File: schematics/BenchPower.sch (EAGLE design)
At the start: 29 parts, among them U1 V_REG_317SINK, X2 9090-4R

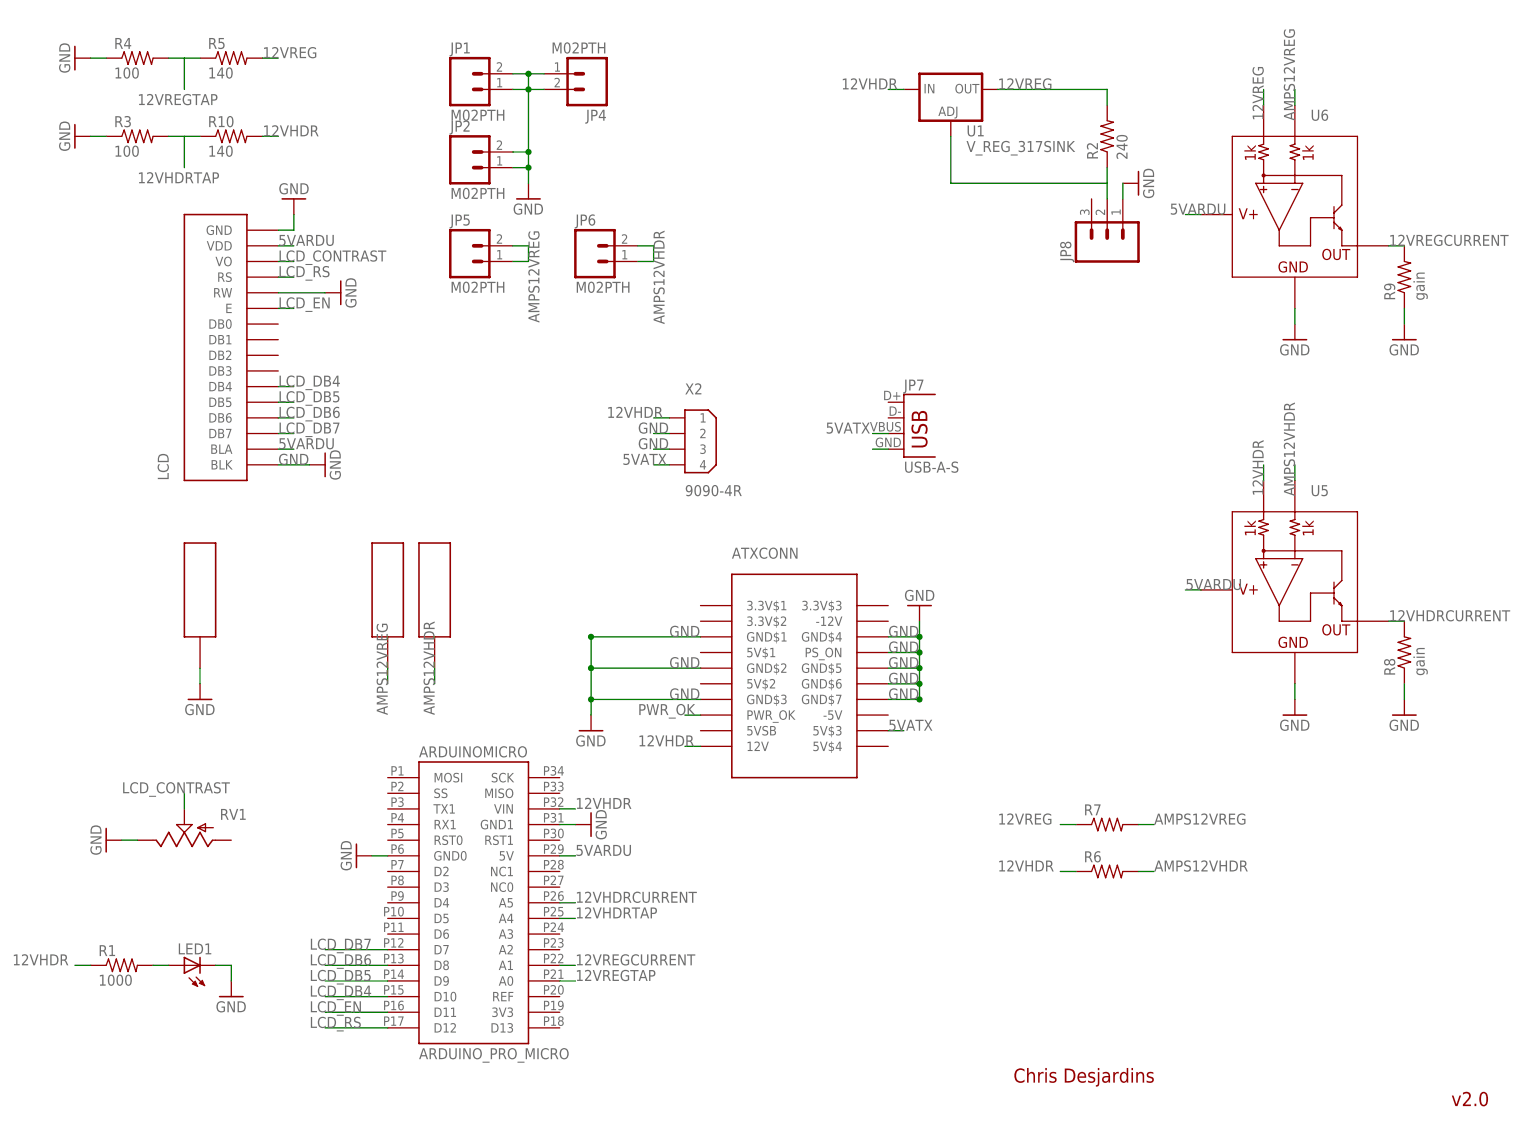
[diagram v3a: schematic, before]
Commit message: Reroute the lcd
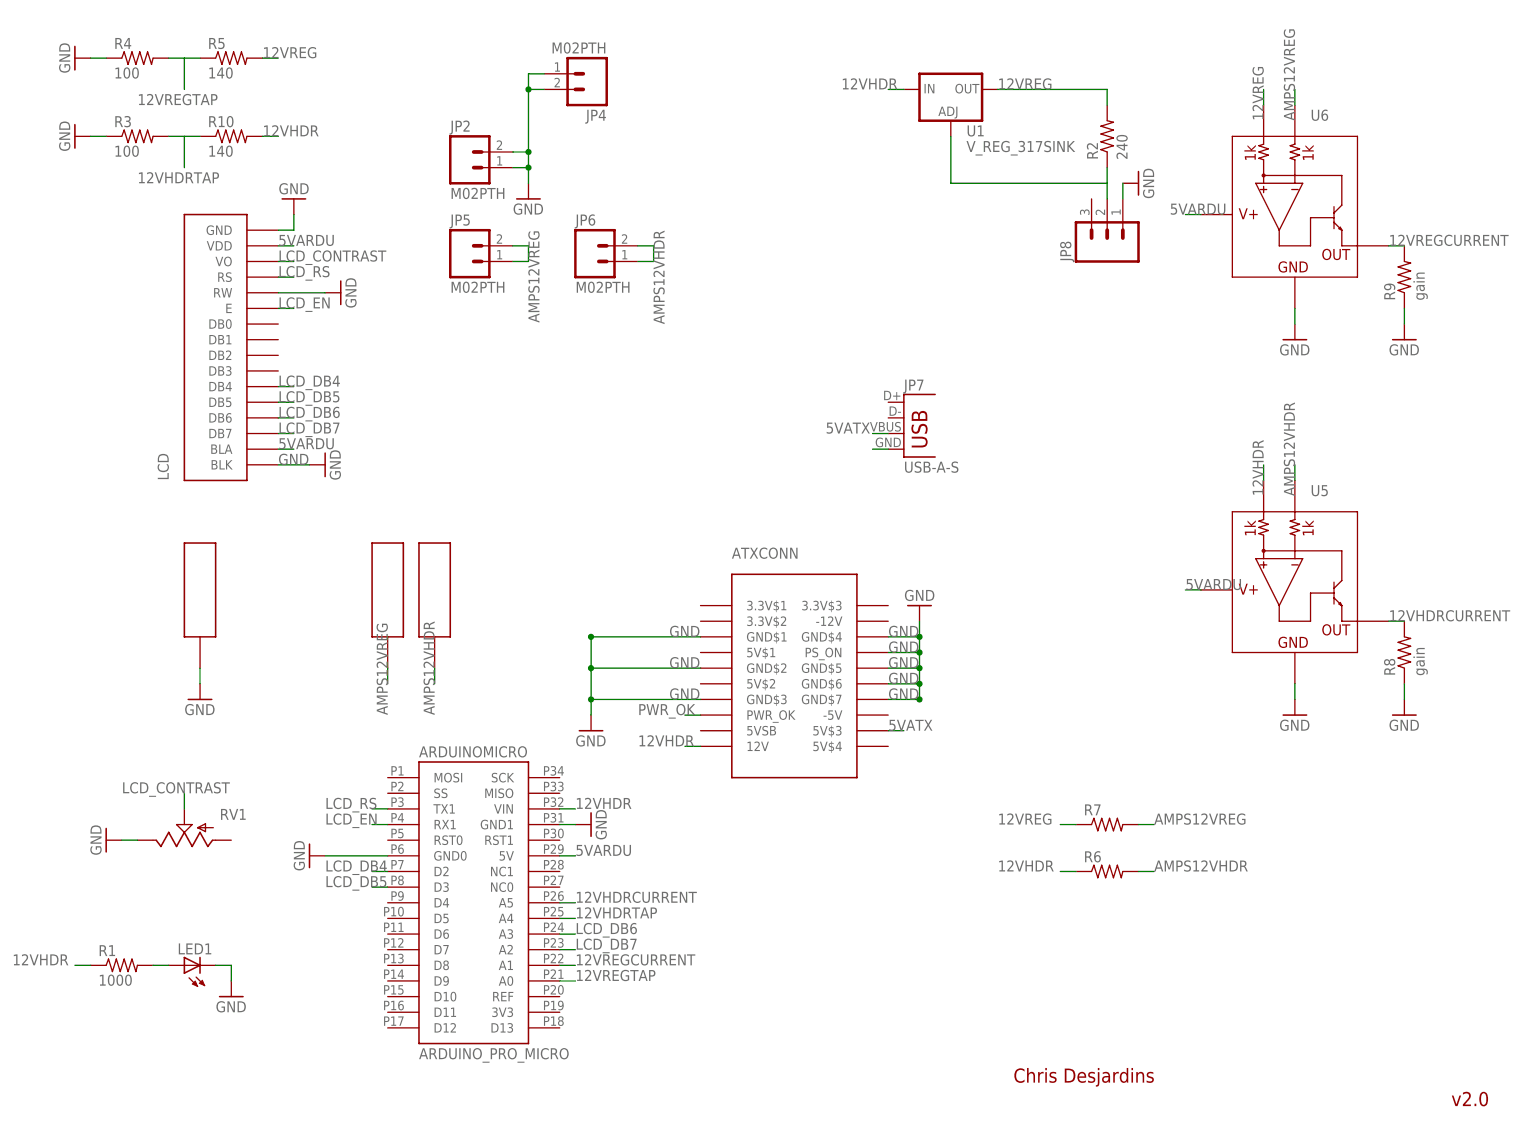
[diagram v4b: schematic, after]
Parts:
- removed JP1: M02PTH, SparkFun-Connectors:M02PTH
- removed X2: 9090-4R, con-thomas-betts:9090-4R
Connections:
- net 12VHDR: no longer X2.1
- net 5VATX: no longer X2.4
- net GND: no longer JP1.1, JP1.2, X2.2, X2.3
- net LCD_DB4: now also ARDUINOMICRO.D2; no longer ARDUINOMICRO.D10
- net LCD_DB5: now also ARDUINOMICRO.D3; no longer ARDUINOMICRO.D9
- net LCD_DB6: now also ARDUINOMICRO.A3; no longer ARDUINOMICRO.D8
- net LCD_DB7: now also ARDUINOMICRO.A2; no longer ARDUINOMICRO.D7
- net LCD_EN: now also ARDUINOMICRO.RX1; no longer ARDUINOMICRO.D11
- net LCD_RS: now also ARDUINOMICRO.TX1; no longer ARDUINOMICRO.D12
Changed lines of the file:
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@@
 <part name="U$5" library="desjardins" deviceset="BINDINGPOST" device=""/>
 <part name="GND1" library="SparkFun-Aesthetics" deviceset="GND" device=""/>
-<part name="X2" library="con-thomas-betts" deviceset="9090-4" device="R"/>
 <part name="ATXCONN" library="desjardins" deviceset="ATXPOWER" device=""/>
 <part name="ARDUINOMICRO" library="ChrisD" deviceset="ARDUINO_PRO_MICRO" device=""/>
@@
 <part name="GND17" library="SparkFun-Aesthetics" deviceset="GND" device=""/>
 <part name="GND18" library="SparkFun-Aesthetics" deviceset="GND" device=""/>
-<part name="JP1" library="SparkFun-Connectors" deviceset="M02" device="PTH"/>
 <part name="U5" library="SparkFun-AnalogIC" deviceset="INA139" device=""/>
 <part name="U6" library="SparkFun-AnalogIC" deviceset="INA139" device=""/>
@@
 <instance part="U$5" gate="G$1" x="33.02" y="91.44"/>
 <instance part="GND1" gate="1" x="33.02" y="73.66"/>
-<instance part="X2" gate="G$1" x="111.76" y="114.3"/>
 <instance part="ATXCONN" gate="G$1" x="129.54" y="76.2"/>
 <instance part="ARDUINOMICRO" gate="G$1" x="76.2" y="45.72"/>
@@
 <instance part="LED1" gate="G$1" x="30.48" y="30.48" rot="R90"/>
 <instance part="GND11" gate="1" x="96.52" y="53.34" rot="R90"/>
-<instance part="GND12" gate="1" x="58.42" y="48.26" rot="R270"/>
+<instance part="GND12" gate="1" x="50.8" y="48.26" rot="R270"/>
 <instance part="R6" gate="G$1" x="180.34" y="45.72"/>
 <instance part="R7" gate="G$1" x="180.34" y="53.34"/>
@@
 <instance part="GND17" gate="1" x="17.78" y="50.8" rot="R270"/>
 <instance part="GND18" gate="1" x="86.36" y="154.94"/>
-<instance part="JP1" gate="G$1" x="76.2" y="172.72"/>
 <instance part="U5" gate="G$1" x="203.2" y="93.98"/>
 <instance part="U6" gate="G$1" x="203.2" y="154.94"/>
@@
 </segment>
 <segment>
-<pinref part="X2" gate="G$1" pin="2"/>
-<wire x1="109.22" y1="116.84" x2="106.68" y2="116.84" width="0.1524" layer="91"/>
-<label x="104.14" y="116.84" size="1.778" layer="95"/>
-</segment>
-<segment>
-<pinref part="X2" gate="G$1" pin="3"/>
-<wire x1="109.22" y1="114.3" x2="106.68" y2="114.3" width="0.1524" layer="91"/>
-<label x="104.14" y="114.3" size="1.778" layer="95"/>
-</segment>
-<segment>
 <pinref part="LCD" gate="G$1" pin="GND"/>
 <wire x1="45.72" y1="149.86" x2="48.26" y2="149.86" width="0.1524" layer="91"/>
@@
 <segment>
 <pinref part="ARDUINOMICRO" gate="G$1" pin="GND0"/>
-<wire x1="63.5" y1="48.26" x2="60.96" y2="48.26" width="0.1524" layer="91"/>
+<wire x1="63.5" y1="48.26" x2="53.34" y2="48.26" width="0.1524" layer="91"/>
 <pinref part="GND12" gate="1" pin="GND"/>
 </segment>
@@
 </segment>
 <segment>
-<pinref part="JP1" gate="G$1" pin="2"/>
-<wire x1="83.82" y1="175.26" x2="86.36" y2="175.26" width="0.1524" layer="91"/>
 <pinref part="GND18" gate="1" pin="GND"/>
 <wire x1="86.36" y1="175.26" x2="86.36" y2="172.72" width="0.1524" layer="91"/>
-<pinref part="JP1" gate="G$1" pin="1"/>
 <wire x1="86.36" y1="172.72" x2="86.36" y2="162.56" width="0.1524" layer="91"/>
 <wire x1="86.36" y1="162.56" x2="86.36" y2="160.02" width="0.1524" layer="91"/>
 <wire x1="86.36" y1="160.02" x2="86.36" y2="157.48" width="0.1524" layer="91"/>
-<wire x1="83.82" y1="172.72" x2="86.36" y2="172.72" width="0.1524" layer="91"/>
 <junction x="86.36" y="172.72"/>
 <pinref part="JP4" gate="G$1" pin="1"/>
@@
 <junction x="86.36" y="160.02"/>
 <junction x="86.36" y="162.56"/>
-<junction x="86.36" y="175.26"/>
 </segment>
 <segment>
@@
 <wire x1="114.3" y1="66.04" x2="111.76" y2="66.04" width="0.1524" layer="91"/>
 <label x="104.14" y="66.04" size="1.778" layer="95"/>
-</segment>
-<segment>
-<pinref part="X2" gate="G$1" pin="1"/>
-<wire x1="109.22" y1="119.38" x2="106.68" y2="119.38" width="0.1524" layer="91"/>
-<label x="99.06" y="119.38" size="1.778" layer="95"/>
 </segment>
 <segment>
@@
 </segment>
 <segment>
-<pinref part="ARDUINOMICRO" gate="G$1" pin="D12"/>
-<wire x1="63.5" y1="20.32" x2="53.34" y2="20.32" width="0.1524" layer="91"/>
-<label x="50.8" y="20.32" size="1.778" layer="95"/>
+<pinref part="ARDUINOMICRO" gate="G$1" pin="TX1"/>
+<wire x1="63.5" y1="55.88" x2="60.96" y2="55.88" width="0.1524" layer="91"/>
+<label x="53.34" y="55.88" size="1.778" layer="95"/>
 </segment>
 </net>
@@
 </segment>
 <segment>
-<pinref part="ARDUINOMICRO" gate="G$1" pin="D11"/>
-<wire x1="63.5" y1="22.86" x2="53.34" y2="22.86" width="0.1524" layer="91"/>
-<label x="50.8" y="22.86" size="1.778" layer="95"/>
+<pinref part="ARDUINOMICRO" gate="G$1" pin="RX1"/>
+<wire x1="63.5" y1="53.34" x2="60.96" y2="53.34" width="0.1524" layer="91"/>
+<label x="53.34" y="53.34" size="1.778" layer="95"/>
 </segment>
 </net>
@@
 </segment>
 <segment>
-<pinref part="ARDUINOMICRO" gate="G$1" pin="D7"/>
-<wire x1="63.5" y1="33.02" x2="53.34" y2="33.02" width="0.1524" layer="91"/>
-<label x="50.8" y="33.02" size="1.778" layer="95"/>
+<pinref part="ARDUINOMICRO" gate="G$1" pin="A2"/>
+<wire x1="91.44" y1="33.02" x2="93.98" y2="33.02" width="0.1524" layer="91"/>
+<label x="93.98" y="33.02" size="1.778" layer="95"/>
 </segment>
 </net>
@@
 </segment>
 <segment>
-<pinref part="ARDUINOMICRO" gate="G$1" pin="D8"/>
-<wire x1="63.5" y1="30.48" x2="53.34" y2="30.48" width="0.1524" layer="91"/>
-<label x="50.8" y="30.48" size="1.778" layer="95"/>
+<pinref part="ARDUINOMICRO" gate="G$1" pin="A3"/>
+<wire x1="91.44" y1="35.56" x2="93.98" y2="35.56" width="0.1524" layer="91"/>
+<label x="93.98" y="35.56" size="1.778" layer="95"/>
 </segment>
 </net>
@@
 </segment>
 <segment>
-<pinref part="ARDUINOMICRO" gate="G$1" pin="D9"/>
-<wire x1="63.5" y1="27.94" x2="53.34" y2="27.94" width="0.1524" layer="91"/>
-<label x="50.8" y="27.94" size="1.778" layer="95"/>
+<pinref part="ARDUINOMICRO" gate="G$1" pin="D3"/>
+<wire x1="63.5" y1="43.18" x2="60.96" y2="43.18" width="0.1524" layer="91"/>
+<label x="53.34" y="43.18" size="1.778" layer="95"/>
 </segment>
 </net>
@@
 </segment>
 <segment>
-<pinref part="ARDUINOMICRO" gate="G$1" pin="D10"/>
-<wire x1="63.5" y1="25.4" x2="53.34" y2="25.4" width="0.1524" layer="91"/>
-<label x="50.8" y="25.4" size="1.778" layer="95"/>
+<pinref part="ARDUINOMICRO" gate="G$1" pin="D2"/>
+<wire x1="63.5" y1="45.72" x2="60.96" y2="45.72" width="0.1524" layer="91"/>
+<label x="53.34" y="45.72" size="1.778" layer="95"/>
 </segment>
 </net>
@@
 <label x="134.62" y="116.84" size="1.778" layer="95"/>
 </segment>
-<segment>
-<pinref part="X2" gate="G$1" pin="4"/>
-<wire x1="109.22" y1="111.76" x2="106.68" y2="111.76" width="0.1524" layer="91"/>
-<label x="101.6" y="111.76" size="1.778" layer="95"/>
-</segment>
-</net>
+</net>

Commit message: New layout
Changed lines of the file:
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@@
 <part name="JP8" library="SparkFun-Connectors" deviceset="M03" device="PTH"/>
 <part name="GND4" library="SparkFun-Aesthetics" deviceset="GND" device=""/>
+<part name="GND14" library="SparkFun-Aesthetics" deviceset="GND" device=""/>
 </parts>
 <sheets>
@@
 <instance part="JP8" gate="G$1" x="180.34" y="147.32" rot="R90"/>
 <instance part="GND4" gate="1" x="185.42" y="157.48" rot="R90"/>
+<instance part="GND14" gate="1" x="139.7" y="114.3" rot="R270"/>
 </instances>
 <busses>
@@
 <pinref part="JP7" gate="G$1" pin="GND"/>
 <wire x1="144.78" y1="114.3" x2="142.24" y2="114.3" width="0.1524" layer="91"/>
+<pinref part="GND14" gate="1" pin="GND"/>
 </segment>
 <segment>
@@
 <wire x1="180.34" y1="157.48" x2="180.34" y2="154.94" width="0.1524" layer="91"/>
 <pinref part="JP8" gate="G$1" pin="2"/>
+<junction x="180.34" y="157.48"/>
 </segment>
 </net>
@@
 <wire x1="30.48" y1="177.8" x2="30.48" y2="172.72" width="0.1524" layer="91"/>
 <label x="22.86" y="170.18" size="1.778" layer="95"/>
+<junction x="30.48" y="177.8"/>
 </segment>
 </net>
@@
 <wire x1="30.48" y1="165.1" x2="30.48" y2="160.02" width="0.1524" layer="91"/>
 <label x="22.86" y="157.48" size="1.778" layer="95"/>
-</segment>
-</net>
+<junction x="30.48" y="165.1"/>
+</segment>
+</net>

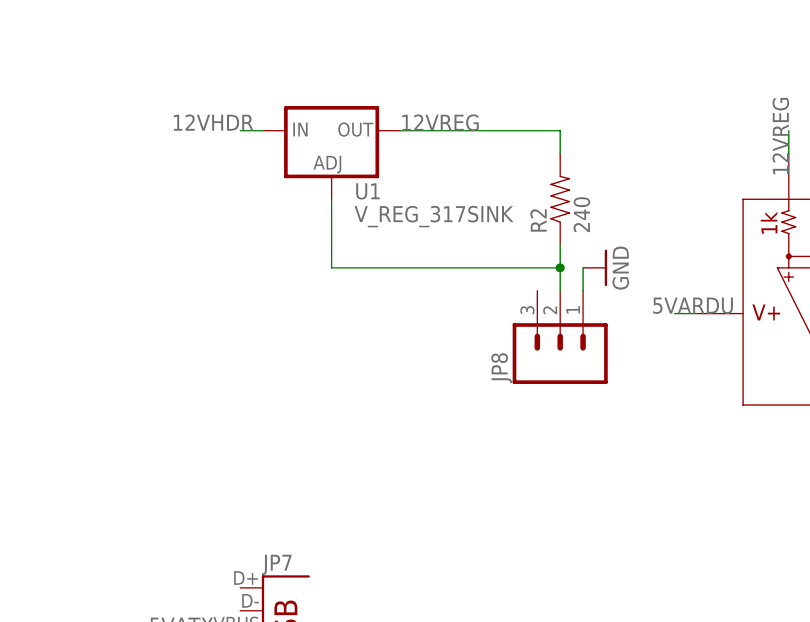
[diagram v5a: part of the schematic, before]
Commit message: Make 12v or 5v selectable into regulator
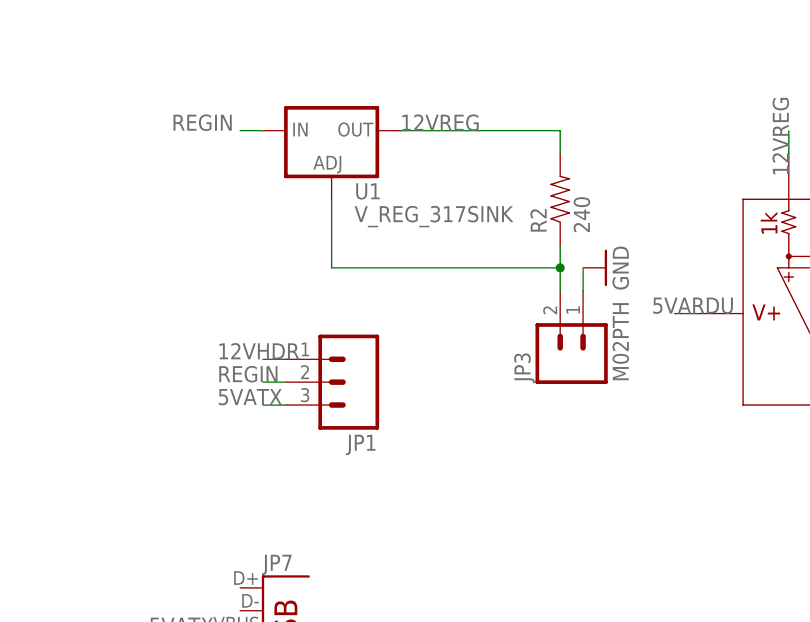
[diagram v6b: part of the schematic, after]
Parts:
- removed JP8: (no value), SparkFun-Connectors:M03PTH
- added JP1: (no value), SparkFun-Connectors:M03PTH
- added JP3: M02PTH, SparkFun-Connectors:M02PTH
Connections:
- new net REGIN: JP1.2, U1.IN
- net 12VHDR: now also JP1.1; no longer U1.IN
- net 5VATX: now also JP1.3
- net ADJREG1: now also JP3.2; no longer JP8.2
- net GND: now also JP3.1; no longer JP8.1
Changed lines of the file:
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@@
 <part name="JP6" library="SparkFun-Connectors" deviceset="M02" device="PTH"/>
 <part name="JP7" library="SparkFun-Connectors" deviceset="USB" device="-A-S"/>
-<part name="JP8" library="SparkFun-Connectors" deviceset="M03" device="PTH"/>
 <part name="GND4" library="SparkFun-Aesthetics" deviceset="GND" device=""/>
 <part name="GND14" library="SparkFun-Aesthetics" deviceset="GND" device=""/>
+<part name="JP1" library="SparkFun-Connectors" deviceset="M03" device="PTH"/>
+<part name="JP3" library="SparkFun-Connectors" deviceset="M02" device="PTH"/>
 </parts>
 <sheets>
@@
 <instance part="JP6" gate="G$1" x="96.52" y="144.78"/>
 <instance part="JP7" gate="G$1" x="147.32" y="114.3"/>
-<instance part="JP8" gate="G$1" x="180.34" y="147.32" rot="R90"/>
 <instance part="GND4" gate="1" x="185.42" y="157.48" rot="R90"/>
 <instance part="GND14" gate="1" x="139.7" y="114.3" rot="R270"/>
+<instance part="JP1" gate="G$1" x="157.48" y="144.78" rot="R180"/>
+<instance part="JP3" gate="G$1" x="182.88" y="147.32" rot="R90"/>
 </instances>
 <busses>
@@
 </segment>
 <segment>
-<pinref part="JP8" gate="G$1" pin="1"/>
-<wire x1="182.88" y1="154.94" x2="182.88" y2="157.48" width="0.1524" layer="91"/>
 <pinref part="GND4" gate="1" pin="GND"/>
+<pinref part="JP3" gate="G$1" pin="1"/>
+<wire x1="182.88" y1="157.48" x2="182.88" y2="154.94" width="0.1524" layer="91"/>
 </segment>
 </net>
@@
 </segment>
 <segment>
-<pinref part="U1" gate="G$1" pin="IN"/>
-<wire x1="147.32" y1="172.72" x2="144.78" y2="172.72" width="0.1524" layer="91"/>
-<label x="137.16" y="172.72" size="1.778" layer="95"/>
-</segment>
-<segment>
 <pinref part="U5" gate="G$1" pin="VIN+"/>
 <wire x1="205.74" y1="109.22" x2="205.74" y2="111.76" width="0.1524" layer="91"/>
 <label x="205.74" y="106.68" size="1.778" layer="95" rot="R90"/>
+</segment>
+<segment>
+<pinref part="JP1" gate="G$1" pin="1"/>
+<wire x1="149.86" y1="147.32" x2="147.32" y2="147.32" width="0.1524" layer="91"/>
+<label x="142.24" y="147.32" size="1.778" layer="95"/>
 </segment>
 </net>
@@
 <pinref part="R2" gate="G$1" pin="1"/>
 <wire x1="180.34" y1="160.02" x2="180.34" y2="157.48" width="0.1524" layer="91"/>
+<pinref part="JP3" gate="G$1" pin="2"/>
 <wire x1="180.34" y1="157.48" x2="180.34" y2="154.94" width="0.1524" layer="91"/>
-<pinref part="JP8" gate="G$1" pin="2"/>
 <junction x="180.34" y="157.48"/>
 </segment>
@@
 <label x="134.62" y="116.84" size="1.778" layer="95"/>
 </segment>
-</net>
+<segment>
+<pinref part="JP1" gate="G$1" pin="3"/>
+<wire x1="149.86" y1="142.24" x2="147.32" y2="142.24" width="0.1524" layer="91"/>
+<label x="142.24" y="142.24" size="1.778" layer="95"/>
+</segment>
+</net>
+<net name="REGIN" class="0">
+<segment>
+<pinref part="U1" gate="G$1" pin="IN"/>
+<wire x1="147.32" y1="172.72" x2="144.78" y2="172.72" width="0.1524" layer="91"/>
+<label x="137.16" y="172.72" size="1.778" layer="95"/>
+</segment>
+<segment>
+<pinref part="JP1" gate="G$1" pin="2"/>
+<wire x1="149.86" y1="144.78" x2="147.32" y2="144.78" width="0.1524" layer="91"/>
+<label x="142.24" y="144.78" size="1.778" layer="95"/>
+</segment>
+</net>
